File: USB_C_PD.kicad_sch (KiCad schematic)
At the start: 24 parts, among them J1 USB_C_Receptacle_USB2.0_14P, U10 AT24C512C-SSHM, U12 TVS2200DRV, U9 PTPS25751SRSMR

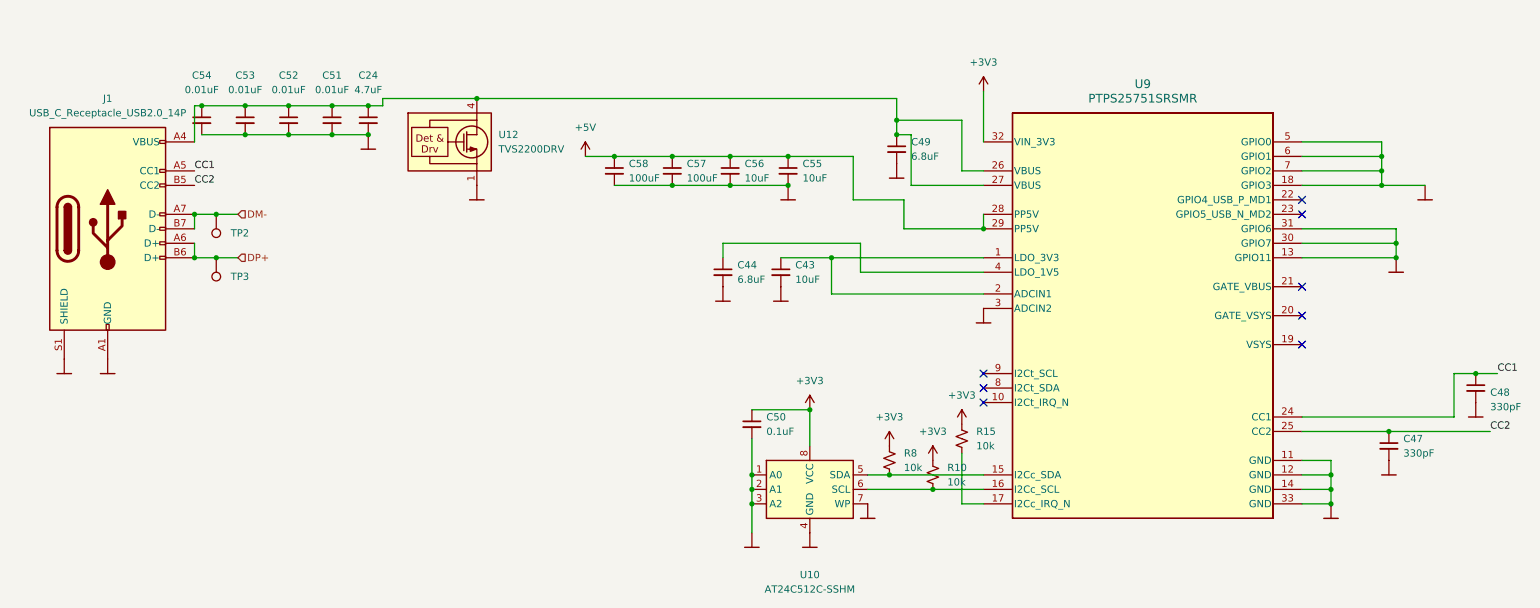
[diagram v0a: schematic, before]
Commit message: added footprints, minor deletions
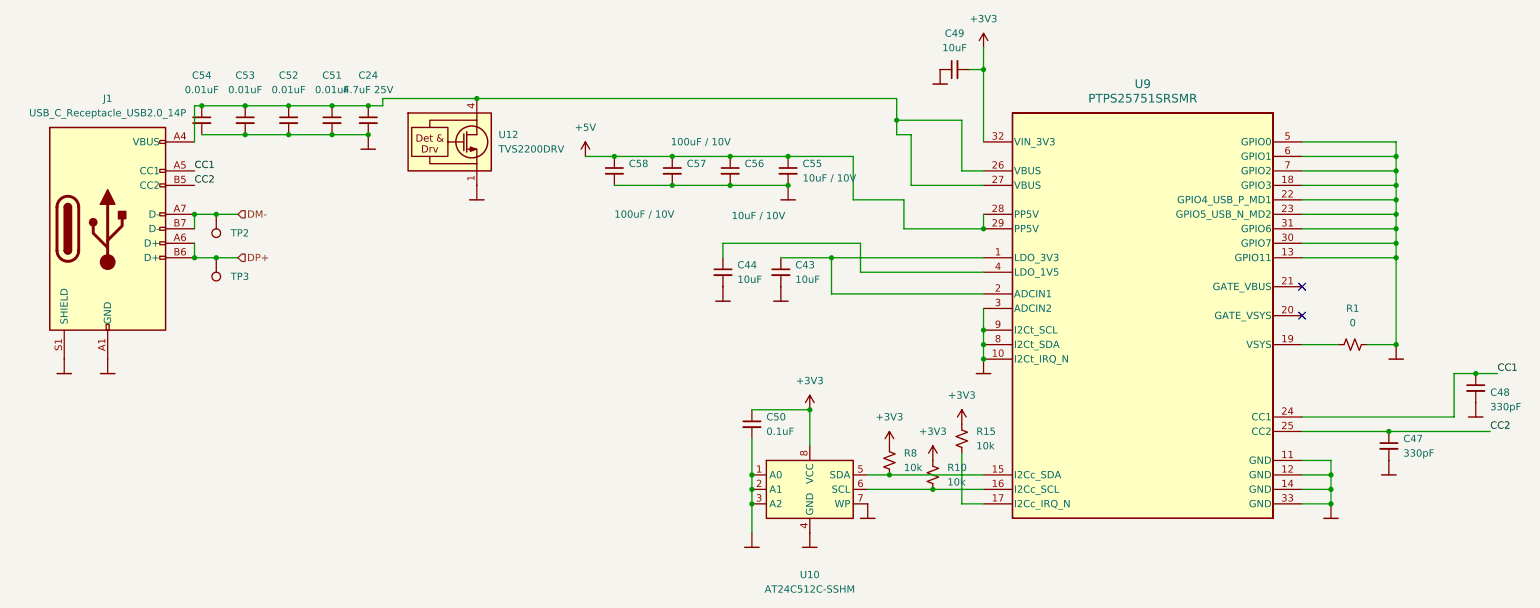
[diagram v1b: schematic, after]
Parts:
- added R1: 0, Resistor_SMD:R_0402_1005Metric, symbol Device:R_Small_US
- C24: value 4.7uF -> 4.7uF 25V; footprint (none) -> Capacitor_SMD:C_0805_2012Metric
- C43, C47, C48, C50, C51, C52, C53, C54: footprint (none) -> Capacitor_SMD:C_0402_1005Metric
- C44, C49: value 6.8uF -> 10uF; footprint (none) -> Capacitor_SMD:C_0402_1005Metric
- C55, C56: value 10uF -> 10uF / 10V; footprint (none) -> Capacitor_SMD:C_0603_1608Metric
- C57, C58: value 100uF -> 100uF / 10V; footprint (none) -> Capacitor_SMD:CP_Elec_5x5.4
- R10, R15, R8: footprint (none) -> Resistor_SMD:R_0402_1005Metric
- U9: footprint RSM0032B-IPC_A -> TPS25751S:RSM0032B-IPC_A
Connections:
- net +3V3: now also C49.2
- net at U9.10 (I2Ct_IRQ_N): now also U9.3 (ADCIN2), U9.8 (I2Ct_SDA), U9.9 (I2Ct_SCL)
- net at U9.13 (GPIO11), U9.30 (GPIO7), U9.31 (GPIO6): now also U9.18 (GPIO3), U9.22 (GPIO4_USB_P_MD1), U9.23 (GPIO5_USB_N_MD2), U9.5 (GPIO0), U9.6 (GPIO1), U9.7 (GPIO2), R1.1
- net at U9.19 (VSYS): now also R1.2
- net at C24.1, C51.1, C52.1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: no longer C49.1
- no-connect marks 8 -> 2

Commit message: add usb-c-pd routing
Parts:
- removed R15: 10k, Resistor_SMD:R_0402_1005Metric, symbol Device:R_Small_US
- removed TP2, TP3: TestPoint, TestPoint:TestPoint_THTPad_1.0x1.0mm_Drill0.5mm, symbol Connector:TestPoint
- added R2: 10K, Resistor_SMD:R_0402_1005Metric, symbol Device:R_Small_US
- R10, R8: value 10k -> 10K
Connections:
- net +3V3: now also R2.1
- net at U10.6 (SCL), U9.16 (I2Cc_SCL): now also R2.2; no longer R10.2
- net at U9.17 (I2Cc_IRQ_N): now also R10.2

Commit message: update capacitors
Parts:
- C57, C58: footprint Capacitor_SMD:CP_Elec_5x5.4 -> Capacitor_SMD:C_1206_3216Metric
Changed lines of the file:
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@@
 			)
 		)
-		(property "Footprint" "Capacitor_SMD:CP_Elec_5x5.4"
+		(property "Footprint" "Capacitor_SMD:C_1206_3216Metric"
 			(at 121.92 50.8 0)
 			(effects
@@
 			)
 		)
-		(property "Footprint" "Capacitor_SMD:CP_Elec_5x5.4"
+		(property "Footprint" "Capacitor_SMD:C_1206_3216Metric"
 			(at 132.08 50.8 0)
 			(effects

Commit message: aaahhhhhh
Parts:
- C47, C48: footprint Capacitor_SMD:C_0402_1005Metric -> Capacitor_SMD:C_0603_1608Metric
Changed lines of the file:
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@@
 			)
 		)
-		(property "Footprint" "Capacitor_SMD:C_0402_1005Metric"
+		(property "Footprint" "Capacitor_SMD:C_0603_1608Metric"
 			(at 257.81 99.06 0)
 			(effects
@@
 			)
 		)
-		(property "Footprint" "Capacitor_SMD:C_0402_1005Metric"
+		(property "Footprint" "Capacitor_SMD:C_0603_1608Metric"
 			(at 273.05 88.9 0)
 			(effects

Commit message: dave's changes
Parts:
- C50: value 0.1uF -> 100nF
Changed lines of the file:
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@@
 			)
 		)
-		(property "Value" "0.1uF"
+		(property "Value" "100nF"
 			(at 148.59 96.5262 0)
 			(effects
